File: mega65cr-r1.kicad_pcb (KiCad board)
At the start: 4 copper layers, 435 x 140 mm, 184 parts, among them J1 DB9_Male_MountingHoles, J10 Molex 46765-2301, J11 CON-SOCJ-2155, J12 Header for power lead to QMTE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, J13 Conn_01x04_Male, J14 Conn_02x17_Odd_Even, J15 696101000002 Fuse Holder 20mm, J16 Conn_01x04_Male, J17 C64_Tape_Port, J18 BA60BC0WT, J19 C64_User_Port, J2 DB9_Male_MountingHoles, J20 C64_Expansion_Port, J21 Audio Header, J22 DB15_Female_HighDensity_Mount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, J23 3.5mm_Stereo_Audio_Jack STX-3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, J24 Component A/V, J25 Joystick Ports Mezannine Lower, J26 Joystick Ports Mezannine Upper, J3 Wuerth_7499010121A, J4 QMTECH FPGA Module U4, J5 QMTECH FPGA Module U5, J6 SDF-60J for IEC 1541 serial p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, J7 QMTECH JTAG, J8 RTC, J9 1140084168 microSD Card Slot, P1 Full-side CD Card Slot, SW1 SW_Push_DPDT, U1 74LS373, U10 74LS06N, U11 74LS06N, U12 DP83826, U13 74LVC374, U14 PTN3363BSMP, U15 LM2678T-5.0, U16 74LVC374, U17 74LVC374, U18 74LS373, U19 74LS373, U2 74LVC374, U20 74LS125, U21 74LS125, U22 74LS06N, U23 74LVC374, U24 74LS125, U25 74LS373, U26 74LS373, U27 74LS138, U28 74LS138, U29 74LS137, U3 74LVC374, U30 74LS137, U31 74LS04, U32 74LVC374, U33 74LVC374, U34 74LVC374, U35 74LS373, U36 74LS373, U37 74LS373, U38 74LVC374, U39 74LVC374, U4 74LS373, U40 74LS373, U41 74LS373, U5 74LS06N, U6 74LVC374, U7 74LVC374, U8 74LS373, U9 74LS373

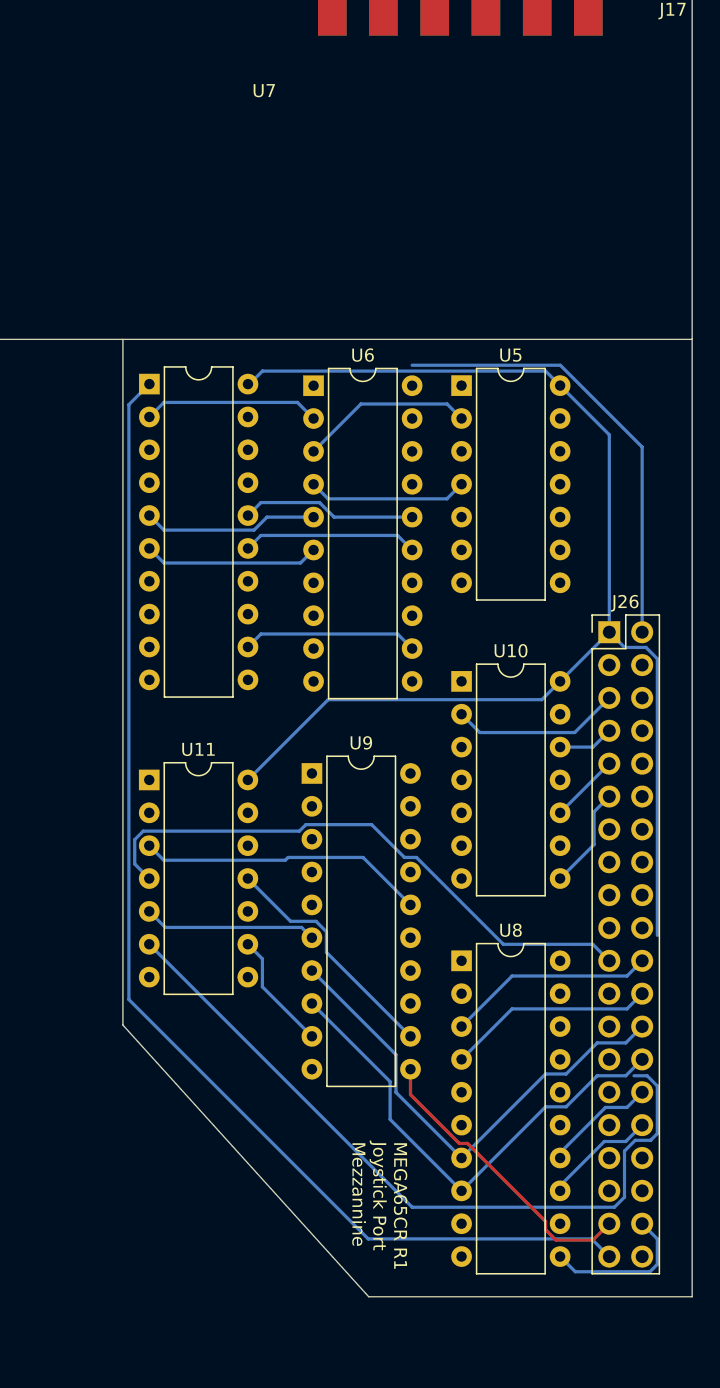
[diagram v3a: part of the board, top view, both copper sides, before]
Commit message: finish laying out joystick mezzannine PCB
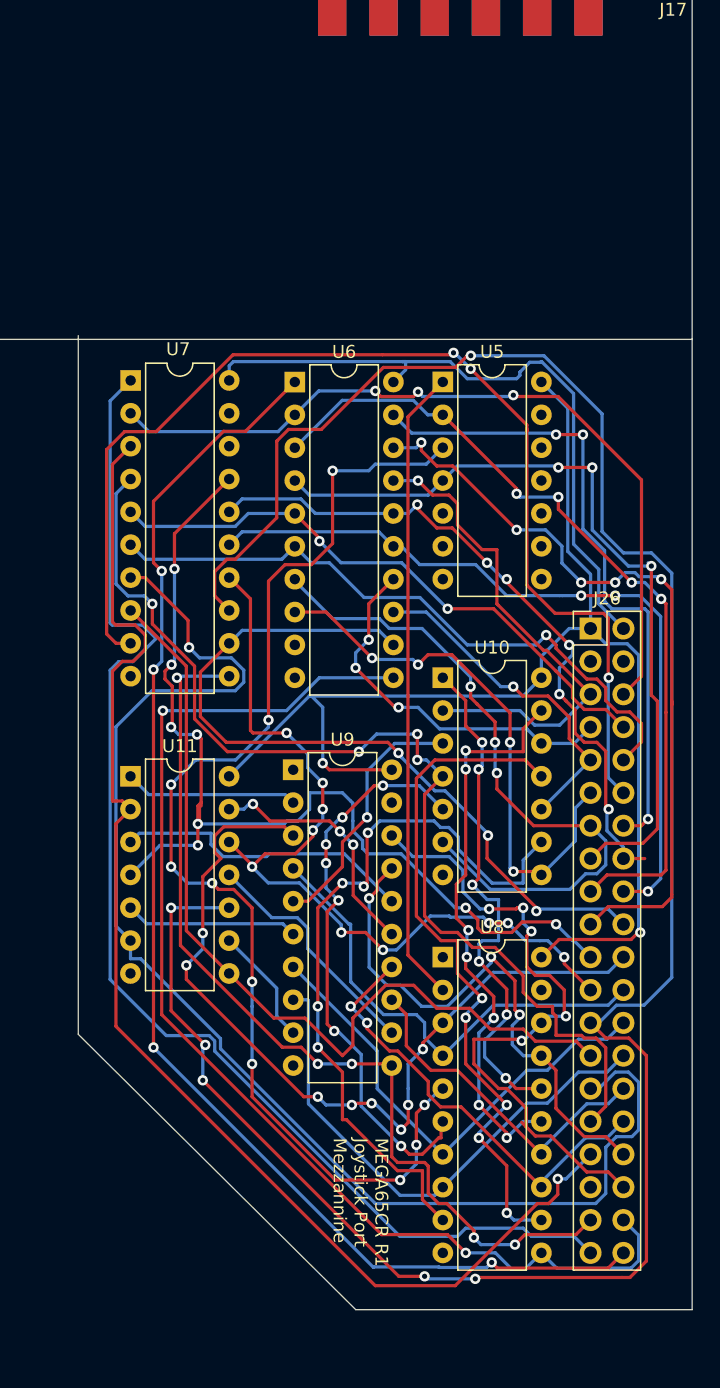
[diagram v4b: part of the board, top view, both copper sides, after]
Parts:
- moved U10 1.48 mm to (445.7, 91.2)
- moved U5 1.48 mm to (445.7, 68.3)
- moved U6 1.48 mm to (434.3, 68.3)
- moved U7 1.48 mm to (421.6, 68.2)
- moved U8 1.48 mm to (445.7, 112.8)
- moved J26 1.48 mm to (457.1, 87.4)
- moved U11 1.48 mm to (421.6, 98.8)
- moved U9 1.48 mm to (434.2, 98.3)
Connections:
- J25 pad 14: MUX_DI4 -> MUX_DI7
- J25 pad 16: MUX_DI5 -> MUX_DI6
- J25 pad 18: MUX_DI6 -> MUX_DI5
- J25 pad 20: MUX_DI7 -> MUX_DI4
- J26 pad 14: /Joystick Ports/M_MUX_DI4 -> /Joystick Ports/M_MUX_DI7
- J26 pad 16: /Joystick Ports/M_MUX_DI5 -> /Joystick Ports/M_MUX_DI6
- J26 pad 18: /Joystick Ports/M_MUX_DI6 -> /Joystick Ports/M_MUX_DI5
- J26 pad 20: /Joystick Ports/M_MUX_DI7 -> /Joystick Ports/M_MUX_DI4
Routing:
- net /Joystick Ports/M_JB_DOWN: track 0.00 -> 182.1 mm, vias 0 -> 6
- net /Joystick Ports/M_MUX_SEL_2_N: track 0.00 -> 101.7 mm, vias 0 -> 4
- net /Joystick Ports/M_JB_AY: track 0.00 -> 100.3 mm, vias 0 -> 1
- net Net-(U5-Pad3): track 0.00 -> 93.0 mm, vias 0 -> 10
- net /Joystick Ports/M_MUX_DI3: track 0.00 -> 88.2 mm, vias 0 -> 3
- net /Joystick Ports/M_JB_AX: track 0.00 -> 83.4 mm, vias 0 -> 4
- net /Joystick Ports/M_MUX_SEL_2: track 11.9 -> 92.3 mm, vias 0 -> 2
- net /Joystick Ports/M_JB_LEFT: track 0.00 -> 67.5 mm
- net /Joystick Ports/M_JB_FIRE: track 0.00 -> 66.1 mm, vias 0 -> 10
- net /Joystick Ports/M_RESET_BTN: track 0.00 -> 59.4 mm, vias 0 -> 5
- net Net-(U10-Pad9): track 0.00 -> 56.9 mm, vias 0 -> 5
- net Net-(U10-Pad11): track 0.00 -> 53.7 mm, vias 0 -> 5
- net /Joystick Ports/M_JA_RIGHT: track 0.00 -> 53.1 mm, vias 0 -> 3
- net /Joystick Ports/M_JA_AY: track 13.4 -> 64.6 mm, vias 0 -> 4
- net /Joystick Ports/M_MUX_DI7: track 0.00 -> 51.1 mm, vias 0 -> 3
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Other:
- outline, holes or cut-outs redrawn
